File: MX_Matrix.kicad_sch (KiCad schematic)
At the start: 34 parts

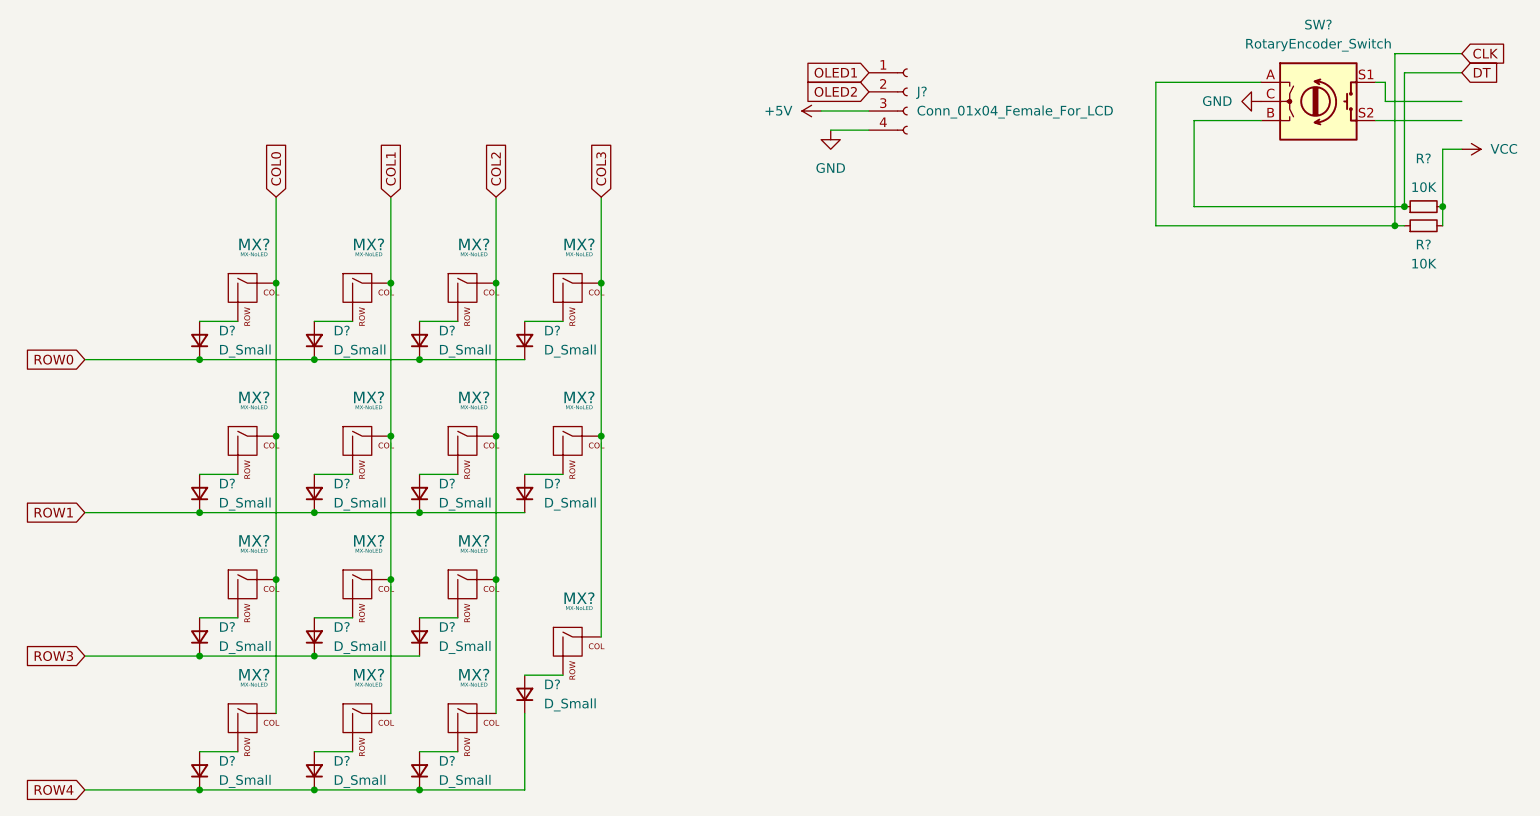
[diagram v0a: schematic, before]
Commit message: schema finished with footprints assigned
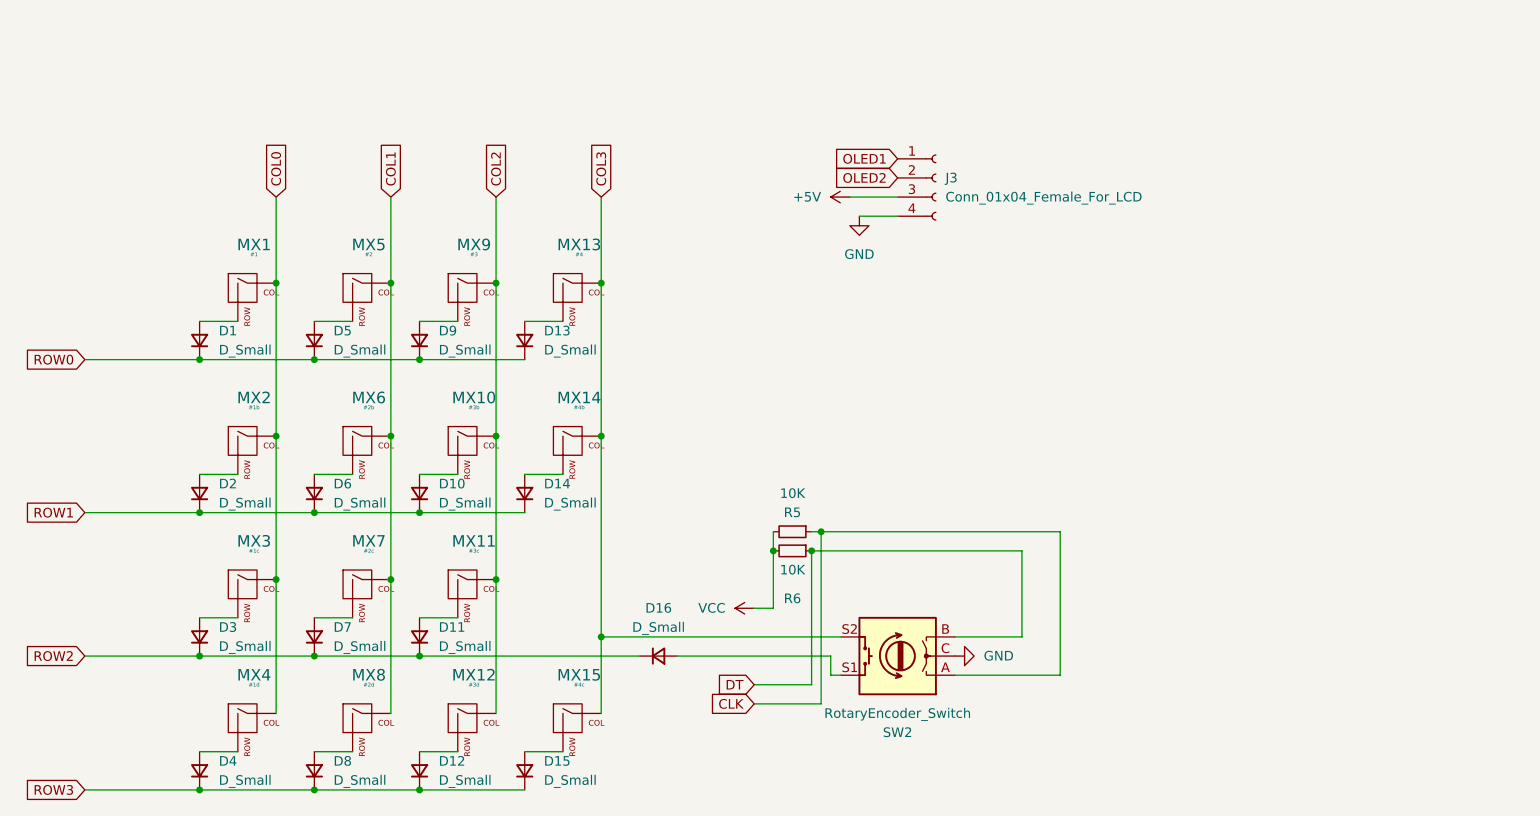
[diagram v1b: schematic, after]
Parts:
- added D16: D_Small, Diode_SMD:D_SOD-123, symbol Device:D_Small
- D1, D10, D11, D12, D13, D14, D15, D2, D3, D4, D5, D6, D7, D8, D9: renamed from D?; footprint (none) -> Diode_SMD:D_SOD-123
- J3: renamed from J?; footprint (none) -> Display:Adafruit_SSD1306
- MX1: renamed from MX?; value MX-NoLED -> #1; footprint (none) -> MX_Alps_Hybrid:MX-1U-NoLED
- MX10: renamed from MX?; value MX-NoLED -> #3b; footprint (none) -> MX_Alps_Hybrid:MX-1U-NoLED
- MX11: renamed from MX?; value MX-NoLED -> #3c; footprint (none) -> MX_Alps_Hybrid:MX-1U-NoLED
- MX12: renamed from MX?; value MX-NoLED -> #3d; footprint (none) -> MX_Alps_Hybrid:MX-1U-NoLED
- MX13: renamed from MX?; value MX-NoLED -> #4; footprint (none) -> MX_Alps_Hybrid:MX-1U-NoLED
- MX14: renamed from MX?; value MX-NoLED -> #4b; footprint (none) -> MX_Alps_Hybrid:MX-1U-NoLED
- MX15: renamed from MX?; value MX-NoLED -> #4c; footprint (none) -> MX_Alps_Hybrid:MX-2U-NoLED
- MX2: renamed from MX?; value MX-NoLED -> #1b; footprint (none) -> MX_Alps_Hybrid:MX-1U-NoLED
- MX3: renamed from MX?; value MX-NoLED -> #1c; footprint (none) -> MX_Alps_Hybrid:MX-1U-NoLED
- MX4: renamed from MX?; value MX-NoLED -> #1d; footprint (none) -> MX_Alps_Hybrid:MX-1U-NoLED
- MX5: renamed from MX?; value MX-NoLED -> #2; footprint (none) -> MX_Alps_Hybrid:MX-1U-NoLED
- MX6: renamed from MX?; value MX-NoLED -> #2b; footprint (none) -> MX_Alps_Hybrid:MX-1U-NoLED
- MX7: renamed from MX?; value MX-NoLED -> #2c; footprint (none) -> MX_Alps_Hybrid:MX-1U-NoLED
- MX8: renamed from MX?; value MX-NoLED -> #2d; footprint (none) -> MX_Alps_Hybrid:MX-1U-NoLED
- MX9: renamed from MX?; value MX-NoLED -> #3; footprint (none) -> MX_Alps_Hybrid:MX-1U-NoLED
- R5, R6: renamed from R?; footprint (none) -> Resistor_SMD:R_0805_2012Metric
- SW2: renamed from SW?; footprint (none) -> Rotary_Encoder:RotaryEncoder_Alps_EC11E-Switch_Vertical_H20mm
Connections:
- net ROW4 is gone; now on net ROW3: D12.1 (K), D15.1 (K), D4.1 (K), D8.1 (K)
- net COL3: now also SW2.S2
- net ROW3: no longer D11.1 (K), D3.1 (K), D7.1 (K)
- net at SW2.S1: now also D16.2 (A)
- new net ROW2: D11.1 (K), D16.1 (K), D3.1 (K), D7.1 (K)
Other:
- moved on the sheet: D15, J3, MX15, R5, R6, SW2

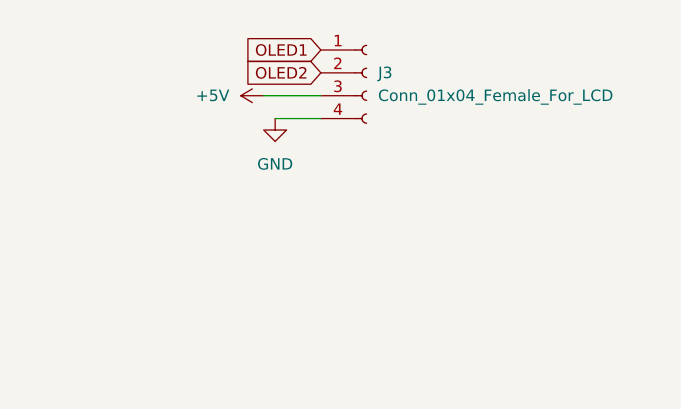
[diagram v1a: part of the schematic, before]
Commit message: fixed annotations and oled footprint
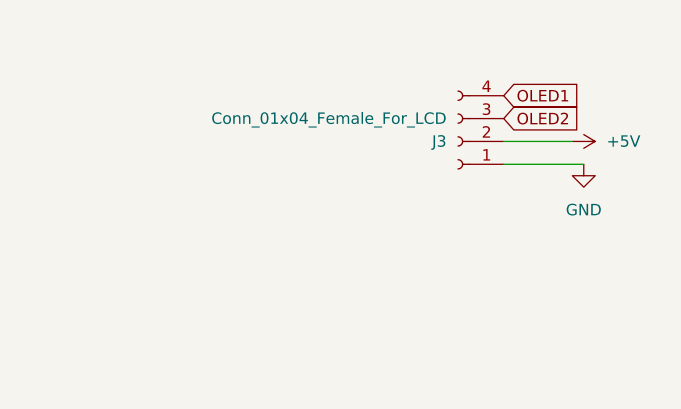
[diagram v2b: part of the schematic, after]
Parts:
- J3: footprint Display:Adafruit_SSD1306 -> Connector_PinHeader_2.54mm:PinHeader_1x04_P2.54mm_Vertical
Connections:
- net +5V: now also J3.2 (Pin_2); no longer J3.3 (Pin_3)
- net GND: now also J3.1 (Pin_1); no longer J3.4 (Pin_4)
- net OLED1: now also J3.4 (Pin_4); no longer J3.1 (Pin_1)
- net OLED2: now also J3.3 (Pin_3); no longer J3.2 (Pin_2)
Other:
- moved on the sheet: J3
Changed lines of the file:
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@@
-    (stroke (width 0) (type default) (color 0 0 0 0))
-  )
-  (wire (pts (xy 166.37 46.99) (xy 172.72 46.99))
     (stroke (width 0) (type default) (color 0 0 0 0))
   )
@@
     (stroke (width 0) (type default) (color 0 0 0 0))
   )
-  (wire (pts (xy 167.64 49.53) (xy 172.72 49.53))
-    (stroke (width 0) (type default) (color 0 0 0 0))
-  )
   (wire (pts (xy 109.22 102.87) (xy 114.3 102.87))
     (stroke (width 0) (type default) (color 0 0 0 0))
@@
     (stroke (width 0) (type default) (color 0 0 0 0))
   )
+  (wire (pts (xy 193.04 52.07) (xy 200.66 52.07))
+    (stroke (width 0) (type default) (color 0 0 0 0))
+  )
   (wire (pts (xy 123.19 83.82) (xy 128.27 83.82))
     (stroke (width 0) (type default) (color 0 0 0 0))
@@
     (stroke (width 0) (type default) (color 0 0 0 0))
   )
+  (wire (pts (xy 193.04 54.61) (xy 201.93 54.61))
+    (stroke (width 0) (type default) (color 0 0 0 0))
+  )
   (wire (pts (xy 64.77 125.73) (xy 80.01 125.73))
     (stroke (width 0) (type default) (color 0 0 0 0))
@@
     (stroke (width 0) (type default) (color 0 0 0 0))
   )
-  (global_label "OLED1" (shape input) (at 172.72 41.91 180) (fields_autoplaced)
-    (effects (font (size 1.27 1.27)) (justify right))
-    (property "Intersheet References" "${INTERSHEET_REFS}" (id 0) (at 164.3198 41.8306 0)
-      (effects (font (size 1.27 1.27)) (justify right) hide)
+  (global_label "OLED1" (shape input) (at 193.04 46.99 0) (fields_autoplaced)
+    (effects (font (size 1.27 1.27)) (justify left))
+    (property "Intersheet References" "${INTERSHEET_REFS}" (id 0) (at 201.4402 47.0694 0)
+      (effects (font (size 1.27 1.27)) (justify left) hide)
     )
   )
@@
     )
   )
-  (global_label "OLED2" (shape input) (at 172.72 44.45 180) (fields_autoplaced)
-    (effects (font (size 1.27 1.27)) (justify right))
-    (property "Intersheet References" "${INTERSHEET_REFS}" (id 0) (at 164.3198 44.3706 0)
-      (effects (font (size 1.27 1.27)) (justify right) hide)
+  (global_label "OLED2" (shape input) (at 193.04 49.53 0) (fields_autoplaced)
+    (effects (font (size 1.27 1.27)) (justify left))
+    (property "Intersheet References" "${INTERSHEET_REFS}" (id 0) (at 201.4402 49.6094 0)
+      (effects (font (size 1.27 1.27)) (justify left) hide)
     )
   )
@@
     (pin "2")
   )
-  (symbol (lib_id "power:+5V") (at 166.37 46.99 90) (unit 1)
-    (in_bom yes) (on_board yes) (fields_autoplaced)
-    (property "Reference" "#PWR0117" (id 0) (at 170.18 46.99 0)
-      (effects (font (size 1.27 1.27)) hide)
-    )
-    (property "Value" "+5V" (id 1) (at 162.56 46.9899 90)
+  (symbol (lib_id "power:+5V") (at 200.66 52.07 270) (unit 1)
+    (in_bom yes) (on_board yes) (fields_autoplaced)
+    (property "Reference" "#PWR0117" (id 0) (at 196.85 52.07 0)
+      (effects (font (size 1.27 1.27)) hide)
+    )
+    (property "Value" "+5V" (id 1) (at 204.47 52.0701 90)
       (effects (font (size 1.27 1.27)) (justify left))
     )
-    (property "Footprint" "" (id 2) (at 166.37 46.99 0)
-      (effects (font (size 1.27 1.27)) hide)
-    )
-    (property "Datasheet" "" (id 3) (at 166.37 46.99 0)
+    (property "Footprint" "" (id 2) (at 200.66 52.07 0)
+      (effects (font (size 1.27 1.27)) hide)
+    )
+    (property "Datasheet" "" (id 3) (at 200.66 52.07 0)
       (effects (font (size 1.27 1.27)) hide)
     )
@@
     (pin "2")
   )
-  (symbol (lib_id "power:GND") (at 167.64 49.53 0) (unit 1)
-    (in_bom yes) (on_board yes) (fields_autoplaced)
-    (property "Reference" "#PWR0118" (id 0) (at 167.64 55.88 0)
-      (effects (font (size 1.27 1.27)) hide)
-    )
-    (property "Value" "GND" (id 1) (at 167.64 54.61 0))
-    (property "Footprint" "" (id 2) (at 167.64 49.53 0)
-      (effects (font (size 1.27 1.27)) hide)
-    )
-    (property "Datasheet" "" (id 3) (at 167.64 49.53 0)
+  (symbol (lib_id "power:GND") (at 201.93 54.61 0) (unit 1)
+    (in_bom yes) (on_board yes) (fields_autoplaced)
+    (property "Reference" "#PWR0118" (id 0) (at 201.93 60.96 0)
+      (effects (font (size 1.27 1.27)) hide)
+    )
+    (property "Value" "GND" (id 1) (at 201.93 59.69 0))
+    (property "Footprint" "" (id 2) (at 201.93 54.61 0)
+      (effects (font (size 1.27 1.27)) hide)
+    )
+    (property "Datasheet" "" (id 3) (at 201.93 54.61 0)
       (effects (font (size 1.27 1.27)) hide)
     )
@@
     (pin "2")
   )
-  (symbol (lib_id "Connector:Conn_01x04_Female") (at 177.8 44.45 0) (unit 1)
-    (in_bom yes) (on_board yes) (fields_autoplaced)
-    (property "Reference" "J3" (id 0) (at 179.07 44.4499 0)
+  (symbol (lib_id "Connector:Conn_01x04_Female") (at 187.96 52.07 180) (unit 1)
+    (in_bom yes) (on_board yes) (fields_autoplaced)
+    (property "Reference" "J3" (id 0) (at 186.69 52.0701 0)
       (effects (font (size 1.27 1.27)) (justify left))
     )
-    (property "Value" "Conn_01x04_Female_For_LCD" (id 1) (at 179.07 46.9899 0)
+    (property "Value" "Conn_01x04_Female_For_LCD" (id 1) (at 186.69 49.5301 0)
       (effects (font (size 1.27 1.27)) (justify left))
     )
-    (property "Footprint" "Display:Adafruit_SSD1306" (id 2) (at 177.8 44.45 0)
-      (effects (font (size 1.27 1.27)) hide)
-    )
-    (property "Datasheet" "~" (id 3) (at 177.8 44.45 0)
-      (effects (font (size 1.27 1.27)) hide)
-    )
+    (property "Footprint" "Connector_PinHeader_2.54mm:PinHeader_1x04_P2.54mm_Vertical" (id 2) (at 187.96 52.07 0)
+      (effects (font (size 1.27 1.27)) hide)
+    )
+    (property "Datasheet" "~" (id 3) (at 187.96 52.07 0)
+      (effects (font (size 1.27 1.27)) hide)
+    )

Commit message: its done
yay
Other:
- company: MIT Liscence -> MIT License
- title: Swithc Layout With LCD & Pot V3 -> Switch Layout With LCD & Pot V3
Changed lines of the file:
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@@
   (paper "A4")
   (title_block
-    (title "Swithc Layout With LCD & Pot V3")
+    (title "Switch Layout With LCD & Pot V3")
     (rev "Rev 3")
-    (company "MIT Liscence")
+    (company "MIT License")
   )
   (junction (at 109.22 125.73) (diameter 0) (color 0 0 0 0)

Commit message: starting rev 3 improvements
now that i have a working prototype making small changes, changed switches to mx only, and cleaned up some routing so far.
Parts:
- MX1, MX10, MX11, MX12, MX13, MX14, MX2, MX3, MX4, MX5, MX6, MX7, MX8, MX9: footprint MX_Alps_Hybrid:MX-1U-NoLED -> MX_Only:MXOnly-1U-NoLED
- MX15: footprint MX_Alps_Hybrid:MX-2U-NoLED -> MX_Only:MXOnly-2U-NoLED
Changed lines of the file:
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@@
       (effects (font (size 0.508 0.508)))
     )
-    (property "Footprint" "MX_Alps_Hybrid:MX-1U-NoLED" (id 2) (at 99.695 80.645 0)
+    (property "Footprint" "MX_Only:MXOnly-1U-NoLED" (id 2) (at 99.695 80.645 0)
       (effects (font (size 1.524 1.524)) hide)
     )
@@
       (effects (font (size 0.508 0.508)))
     )
-    (property "Footprint" "MX_Alps_Hybrid:MX-1U-NoLED" (id 2) (at 85.725 60.325 0)
+    (property "Footprint" "MX_Only:MXOnly-1U-NoLED" (id 2) (at 85.725 60.325 0)
       (effects (font (size 1.524 1.524)) hide)
     )
@@
       (effects (font (size 0.508 0.508)))
     )
-    (property "Footprint" "MX_Alps_Hybrid:MX-1U-NoLED" (id 2) (at 70.485 60.325 0)
+    (property "Footprint" "MX_Only:MXOnly-1U-NoLED" (id 2) (at 70.485 60.325 0)
       (effects (font (size 1.524 1.524)) hide)
     )
@@
       (effects (font (size 0.508 0.508)))
     )
-    (property "Footprint" "MX_Alps_Hybrid:MX-1U-NoLED" (id 2) (at 85.725 99.695 0)
+    (property "Footprint" "MX_Only:MXOnly-1U-NoLED" (id 2) (at 85.725 99.695 0)
       (effects (font (size 1.524 1.524)) hide)
     )
@@
       (effects (font (size 0.508 0.508)))
     )
-    (property "Footprint" "MX_Alps_Hybrid:MX-1U-NoLED" (id 2) (at 85.725 80.645 0)
+    (property "Footprint" "MX_Only:MXOnly-1U-NoLED" (id 2) (at 85.725 80.645 0)
       (effects (font (size 1.524 1.524)) hide)
     )
@@
       (effects (font (size 0.508 0.508)))
     )
-    (property "Footprint" "MX_Alps_Hybrid:MX-1U-NoLED" (id 2) (at 113.665 60.325 0)
+    (property "Footprint" "MX_Only:MXOnly-1U-NoLED" (id 2) (at 113.665 60.325 0)
       (effects (font (size 1.524 1.524)) hide)
     )
@@
       (effects (font (size 0.508 0.508)))
     )
-    (property "Footprint" "MX_Alps_Hybrid:MX-1U-NoLED" (id 2) (at 113.665 80.645 0)
+    (property "Footprint" "MX_Only:MXOnly-1U-NoLED" (id 2) (at 113.665 80.645 0)
       (effects (font (size 1.524 1.524)) hide)
     )
@@
       (effects (font (size 0.508 0.508)))
     )
-    (property "Footprint" "MX_Alps_Hybrid:MX-1U-NoLED" (id 2) (at 70.485 99.695 0)
+    (property "Footprint" "MX_Only:MXOnly-1U-NoLED" (id 2) (at 70.485 99.695 0)
       (effects (font (size 1.524 1.524)) hide)
     )
@@
       (effects (font (size 0.508 0.508)))
     )
-    (property "Footprint" "MX_Alps_Hybrid:MX-1U-NoLED" (id 2) (at 99.695 99.695 0)
+    (property "Footprint" "MX_Only:MXOnly-1U-NoLED" (id 2) (at 99.695 99.695 0)
       (effects (font (size 1.524 1.524)) hide)
     )
@@
       (effects (font (size 0.508 0.508)))
     )
-    (property "Footprint" "MX_Alps_Hybrid:MX-1U-NoLED" (id 2) (at 70.485 80.645 0)
+    (property "Footprint" "MX_Only:MXOnly-1U-NoLED" (id 2) (at 70.485 80.645 0)
       (effects (font (size 1.524 1.524)) hide)
     )
@@
       (effects (font (size 0.508 0.508)))
     )
-    (property "Footprint" "MX_Alps_Hybrid:MX-1U-NoLED" (id 2) (at 99.695 117.475 0)
+    (property "Footprint" "MX_Only:MXOnly-1U-NoLED" (id 2) (at 99.695 117.475 0)
       (effects (font (size 1.524 1.524)) hide)
     )
@@
       (effects (font (size 0.508 0.508)))
     )
-    (property "Footprint" "MX_Alps_Hybrid:MX-2U-NoLED" (id 2) (at 113.665 117.475 0)
+    (property "Footprint" "MX_Only:MXOnly-2U-NoLED" (id 2) (at 113.665 117.475 0)
       (effects (font (size 1.524 1.524)) hide)
     )
@@
       (effects (font (size 0.508 0.508)))
     )
-    (property "Footprint" "MX_Alps_Hybrid:MX-1U-NoLED" (id 2) (at 85.725 117.475 0)
+    (property "Footprint" "MX_Only:MXOnly-1U-NoLED" (id 2) (at 85.725 117.475 0)
       (effects (font (size 1.524 1.524)) hide)
     )
@@
       (effects (font (size 0.508 0.508)))
     )
-    (property "Footprint" "MX_Alps_Hybrid:MX-1U-NoLED" (id 2) (at 99.695 60.325 0)
+    (property "Footprint" "MX_Only:MXOnly-1U-NoLED" (id 2) (at 99.695 60.325 0)
       (effects (font (size 1.524 1.524)) hide)
     )
@@
       (effects (font (size 0.508 0.508)))
     )
-    (property "Footprint" "MX_Alps_Hybrid:MX-1U-NoLED" (id 2) (at 70.485 117.475 0)
-      (effects (font (size 1.524 1.524)) hide)
-    )
+    (property "Footprint" "MX_Only:MXOnly-1U-NoLED" (id 2) (at 70.485 117.475 0)
+      (effects (font (size 1.524 1.524)) hide)
+    )
